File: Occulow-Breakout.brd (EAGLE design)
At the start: 100 x 80 mm, 12 parts, among them X1 SMA-SMD

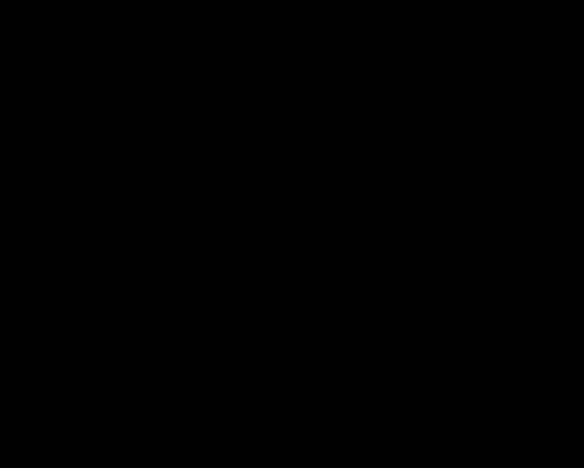
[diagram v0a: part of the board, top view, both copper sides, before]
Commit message: Added PIR sensor
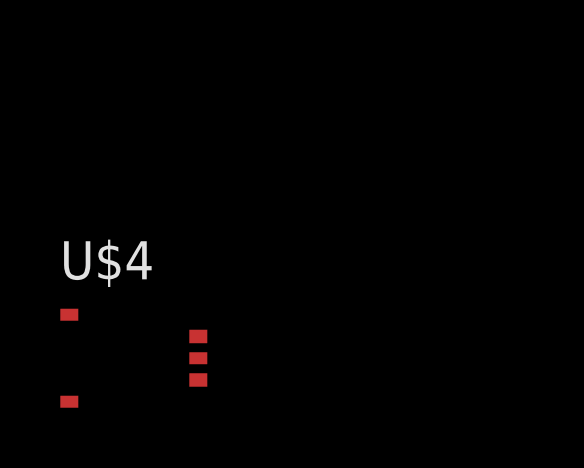
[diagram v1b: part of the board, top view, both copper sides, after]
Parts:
- added U$4: IRS-B210ST01, PIR:IRS-B210ST01
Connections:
- new net LR_CTS: U$1.3
- new net LR_RTS: U$1.2
- new net LR_RX: U$1.7
- new net LR_TX: U$1.6
- net GND: now also U$1.1, U$1.11, U$1.20, U$1.28, U$1.33, U$1.41, U$1.47, U$1.8
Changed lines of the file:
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@@
 </element>
 <element name="U$3" library="SMA-JACK" package="SMA-JACK" value="SMA-JACKFEMALE" x="-107.95" y="-15.24"/>
+<element name="U$4" library="PIR" package="IRS-B210ST01" value="IRS-B210ST01" x="-128.27" y="-25.4"/>
 </elements>
 <signals>
@@
 <contactref element="U$1" pad="22"/>
 <contactref element="U$1" pad="21"/>
+<contactref element="U$1" pad="20"/>
+<contactref element="U$1" pad="11"/>
+<contactref element="U$1" pad="8"/>
+<contactref element="U$1" pad="1"/>
+<contactref element="U$1" pad="28"/>
+<contactref element="U$1" pad="33"/>
+<contactref element="U$1" pad="41"/>
+<contactref element="U$1" pad="47"/>
 <wire x1="-110.49" y1="-12.7" x2="-110.49" y2="-17.78" width="0" layer="19" extent="1-1"/>
 <wire x1="-105.41" y1="-17.78" x2="-110.49" y2="-17.78" width="0" layer="19" extent="1-1"/>
@@
 <wire x1="-40.64" y1="4.57" x2="-105.41" y2="-12.7" width="0" layer="19" extent="1-1"/>
 <wire x1="-39.37" y1="4.57" x2="-40.64" y2="4.57" width="0" layer="19" extent="1-1"/>
-<wire x1="-26.67" y1="27.94" x2="-39.37" y2="4.57" width="0" layer="19" extent="1-1"/>
+<wire x1="-31.75" y1="2.54" x2="-39.37" y2="4.57" width="0" layer="19" extent="1-1"/>
+<wire x1="-31.75" y1="10.16" x2="-31.75" y2="2.54" width="0" layer="19" extent="1-1"/>
+<wire x1="-31.75" y1="20.32" x2="-31.75" y2="10.16" width="0" layer="19" extent="1-1"/>
+<wire x1="-31.75" y1="26.67" x2="-31.75" y2="20.32" width="0" layer="19" extent="1-1"/>
+<wire x1="-26.67" y1="27.94" x2="-31.75" y2="26.67" width="0" layer="19" extent="1-1"/>
 <wire x1="-25.4" y1="27.94" x2="-26.67" y2="27.94" width="0" layer="19" extent="1-1"/>
 <wire x1="-22.86" y1="27.94" x2="-25.4" y2="27.94" width="0" layer="19" extent="1-1"/>
 <wire x1="-20.32" y1="27.94" x2="-22.86" y2="27.94" width="0" layer="19" extent="1-1"/>
 <wire x1="-19.05" y1="27.94" x2="-20.32" y2="27.94" width="0" layer="19" extent="1-1"/>
+<wire x1="-13.97" y1="26.67" x2="-19.05" y2="27.94" width="0" layer="19" extent="1-1"/>
+<wire x1="-13.97" y1="15.24" x2="-13.97" y2="26.67" width="0" layer="19" extent="1-1"/>
+<wire x1="-13.97" y1="11.43" x2="-13.97" y2="15.24" width="0" layer="19" extent="1-1"/>
+<wire x1="-13.97" y1="2.54" x2="-13.97" y2="11.43" width="0" layer="19" extent="1-1"/>
 <wire x1="-22.73" y1="41.91" x2="-22.86" y2="27.94" width="0" layer="19" extent="1-1"/>
 <wire x1="-16.38" y1="41.91" x2="-22.73" y2="41.91" width="0" layer="19" extent="1-1"/>
-<wire x1="-52.222" y1="41.91" x2="-26.67" y2="27.94" width="0" layer="19" extent="1-1"/>
+<wire x1="-52.222" y1="41.91" x2="-31.75" y2="26.67" width="0" layer="19" extent="1-1"/>
 </signal>
 <signal name="N$2">
@@
 <wire x1="-21.59" y1="27.94" x2="-107.95" y2="-15.24" width="0" layer="19" extent="1-1"/>
 </signal>
+<signal name="LR_RX">
+<contactref element="U$1" pad="7"/>
+</signal>
+<signal name="LR_TX">
+<contactref element="U$1" pad="6"/>
+</signal>
+<signal name="LR_CTS">
+<contactref element="U$1" pad="3"/>
+</signal>
+<signal name="LR_RTS">
+<contactref element="U$1" pad="2"/>
+</signal>
 </signals>

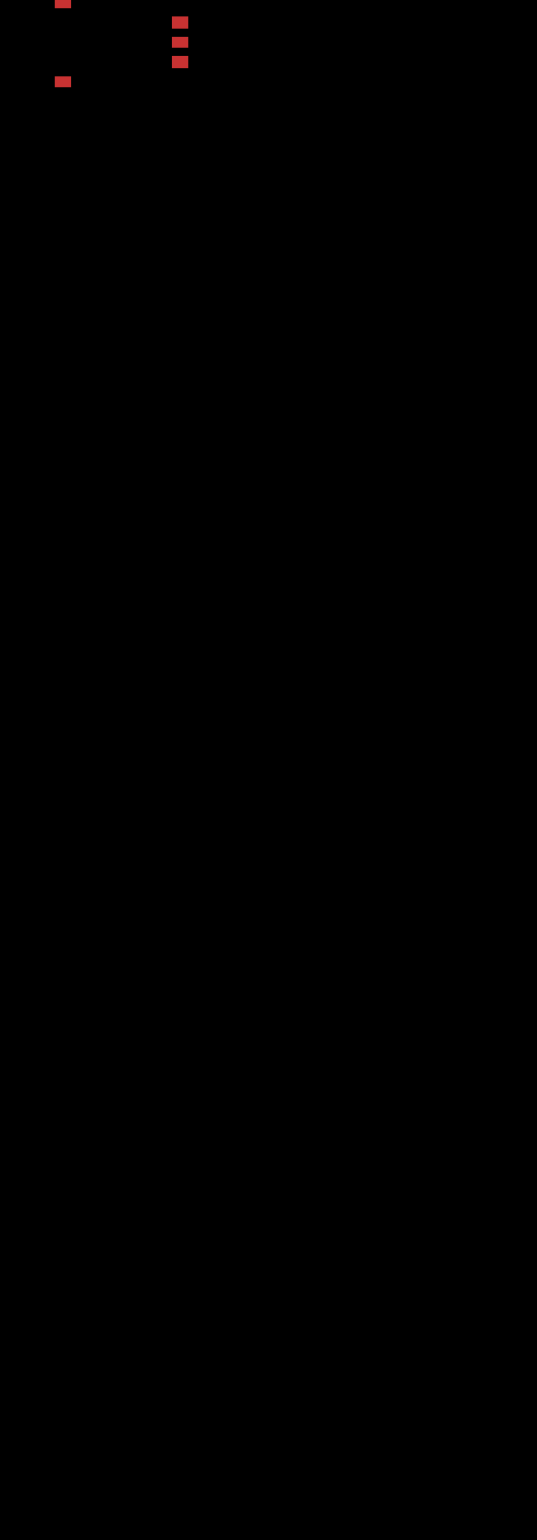
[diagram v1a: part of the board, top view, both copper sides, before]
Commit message: PIR power circuit
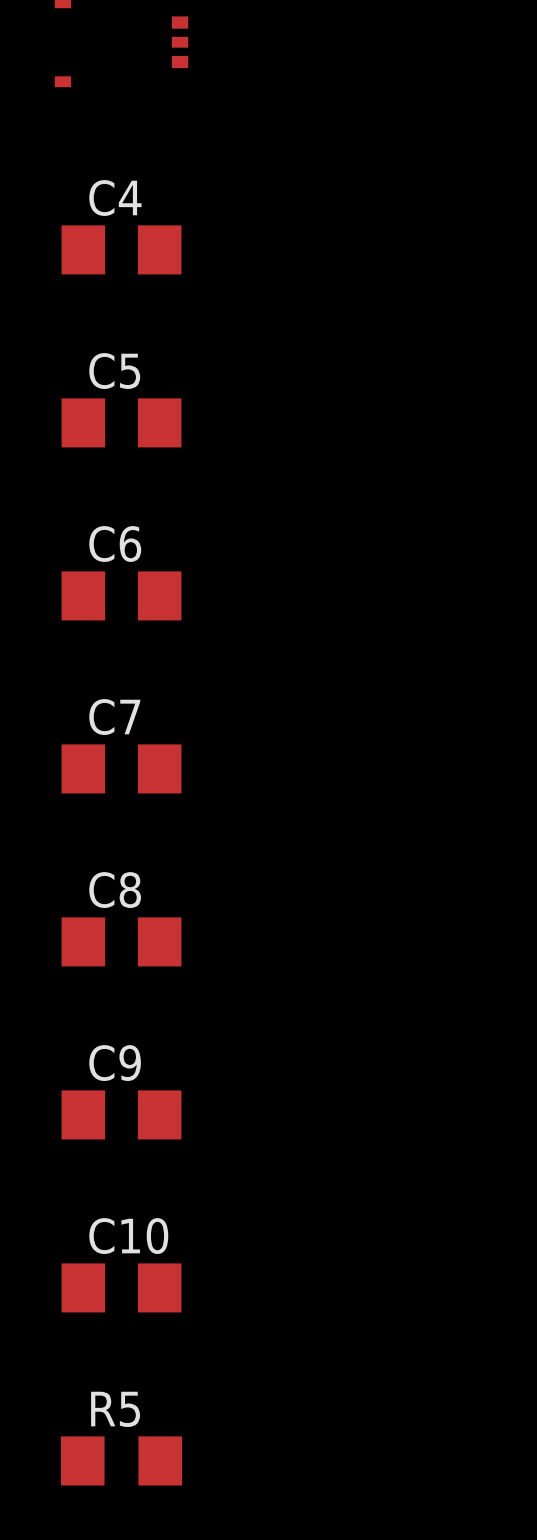
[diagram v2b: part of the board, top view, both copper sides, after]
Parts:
- added C10: 100uF, rcl:C1206
- added C4, C5: 100pF, rcl:C1206
- added C6: 0.01uF, rcl:C1206
- added C7: 0.1uF, rcl:C1206
- added C8: 1uF, rcl:C1206
- added C9: 10uF, rcl:C1206
- added R5: 619k, resistor:R1206
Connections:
- new net N$5: C10.1, C4.1, C5.1, C6.1, C7.1, C8.1, C9.1, R5.1, U$4.3
- new net PIR_OUT: U$4.1
- net GND: now also C10.2, C4.2, C5.2, C6.2, C7.2, C8.2, C9.2, U$4.2, U$4.4, U$4.5
- net VCC: now also R5.2
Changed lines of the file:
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@@
 <element name="U$3" library="SMA-JACK" package="SMA-JACK" value="SMA-JACKFEMALE" x="-107.95" y="-15.24"/>
 <element name="U$4" library="PIR" package="IRS-B210ST01" value="IRS-B210ST01" x="-128.27" y="-25.4"/>
+<element name="C4" library="rcl" package="C1206" value="100pF" x="-128.27" y="-33.02"/>
+<element name="C5" library="rcl" package="C1206" value="100pF" x="-128.27" y="-39.37"/>
+<element name="C6" library="rcl" package="C1206" value="0.01uF" x="-128.27" y="-45.72"/>
+<element name="C7" library="rcl" package="C1206" value="0.1uF" x="-128.27" y="-52.07"/>
+<element name="C8" library="rcl" package="C1206" value="1uF" x="-128.27" y="-58.42"/>
+<element name="C9" library="rcl" package="C1206" value="10uF" x="-128.27" y="-64.77"/>
+<element name="C10" library="rcl" package="C1206" value="100uF" x="-128.27" y="-71.12"/>
+<element name="R5" library="resistor" package="R1206" value="619k" x="-128.27" y="-77.47"/>
 </elements>
 <signals>
@@
 <contactref element="C1" pad="1"/>
 <contactref element="U$2" pad="13"/>
+<contactref element="R5" pad="2"/>
+<wire x1="-44.45" y1="10.67" x2="-126.848" y2="-77.47" width="0" layer="19" extent="1-1"/>
 <wire x1="-39.39" y1="10.67" x2="-44.45" y2="10.67" width="0" layer="19" extent="1-1"/>
 <wire x1="-44.298" y1="41.91" x2="-44.45" y2="10.67" width="0" layer="19" extent="1-1"/>
@@
 <contactref element="U$1" pad="41"/>
 <contactref element="U$1" pad="47"/>
+<contactref element="U$4" pad="4"/>
+<contactref element="U$4" pad="5"/>
+<contactref element="U$4" pad="2"/>
+<contactref element="C4" pad="2"/>
+<contactref element="C5" pad="2"/>
+<contactref element="C6" pad="2"/>
+<contactref element="C7" pad="2"/>
+<contactref element="C8" pad="2"/>
+<contactref element="C9" pad="2"/>
+<contactref element="C10" pad="2"/>
+<wire x1="-126.87" y1="-64.77" x2="-126.87" y2="-71.12" width="0" layer="19" extent="1-1"/>
+<wire x1="-126.87" y1="-58.42" x2="-126.87" y2="-64.77" width="0" layer="19" extent="1-1"/>
+<wire x1="-126.87" y1="-52.07" x2="-126.87" y2="-58.42" width="0" layer="19" extent="1-1"/>
+<wire x1="-126.87" y1="-45.72" x2="-126.87" y2="-52.07" width="0" layer="19" extent="1-1"/>
+<wire x1="-126.87" y1="-39.37" x2="-126.87" y2="-45.72" width="0" layer="19" extent="1-1"/>
+<wire x1="-126.87" y1="-33.02" x2="-126.87" y2="-39.37" width="0" layer="19" extent="1-1"/>
+<wire x1="-130.42" y1="-26.85" x2="-126.87" y2="-33.02" width="0" layer="19" extent="1-1"/>
+<wire x1="-130.42" y1="-23.95" x2="-130.42" y2="-26.85" width="0" layer="19" extent="1-1"/>
+<wire x1="-126.12" y1="-25.4" x2="-130.42" y2="-26.85" width="0" layer="19" extent="1-1"/>
+<wire x1="-110.49" y1="-17.78" x2="-126.12" y2="-25.4" width="0" layer="19" extent="1-1"/>
 <wire x1="-110.49" y1="-12.7" x2="-110.49" y2="-17.78" width="0" layer="19" extent="1-1"/>
 <wire x1="-105.41" y1="-17.78" x2="-110.49" y2="-17.78" width="0" layer="19" extent="1-1"/>
@@
 <contactref element="U$1" pad="2"/>
 </signal>
+<signal name="N$5">
+<contactref element="U$4" pad="3"/>
+<contactref element="C4" pad="1"/>
+<contactref element="C5" pad="1"/>
+<contactref element="C6" pad="1"/>
+<contactref element="C7" pad="1"/>
+<contactref element="C8" pad="1"/>
+<contactref element="C9" pad="1"/>
+<contactref element="C10" pad="1"/>
+<contactref element="R5" pad="1"/>
+<wire x1="-129.67" y1="-71.12" x2="-129.692" y2="-77.47" width="0" layer="19" extent="1-1"/>
+<wire x1="-129.67" y1="-64.77" x2="-129.67" y2="-71.12" width="0" layer="19" extent="1-1"/>
+<wire x1="-129.67" y1="-58.42" x2="-129.67" y2="-64.77" width="0" layer="19" extent="1-1"/>
+<wire x1="-129.67" y1="-52.07" x2="-129.67" y2="-58.42" width="0" layer="19" extent="1-1"/>
+<wire x1="-129.67" y1="-45.72" x2="-129.67" y2="-52.07" width="0" layer="19" extent="1-1"/>
+<wire x1="-129.67" y1="-39.37" x2="-129.67" y2="-45.72" width="0" layer="19" extent="1-1"/>
+<wire x1="-129.67" y1="-33.02" x2="-129.67" y2="-39.37" width="0" layer="19" extent="1-1"/>
+<wire x1="-126.12" y1="-24.675" x2="-129.67" y2="-33.02" width="0" layer="19" extent="1-1"/>
+</signal>
+<signal name="PIR_OUT">
+<contactref element="U$4" pad="1"/>
+</signal>
 </signals>
